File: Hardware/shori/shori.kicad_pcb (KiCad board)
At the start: 4 copper layers, 13 x 1.4 mm, 50 parts, among them J1 Conn_02x03_Top_Bottom, J2 SWD_Header, J3 UART_Header, J5 AudioJack3, U1 STM32F405RGT6, U2 AP2112K-3.3, U3 PCM3060PWR, U4 NE5532, Y1 16MHz

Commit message: Started General Component Layout
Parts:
- moved R2 118.0 mm to (167.8, 125.3), turned to -90 degrees
- moved R3 117.8 mm to (170.2, 125.3), turned to 90 degrees
- moved R1 103.9 mm to (163.8, 105.5), turned to 180 degrees
- moved J2 93.6 mm to (172.8, 100.1), turned to -90 degrees
- moved J3 91.3 mm to (135.0, 111.8), turned to -90 degrees
- moved C12 80.2 mm to (117.7, 98.7)
- moved C18 43.9 mm to (202.8, 116.2), turned to -90 degrees
- moved C15 41.7 mm to (220.5, 115.3), turned to -90 degrees
- moved U3 41.7 mm to (209.6, 116.0)
- moved C17 40.5 mm to (200.0, 116.3), turned to -90 degrees
- moved U1 38.8 mm to (166.5, 115.3)
- moved C16 38.2 mm to (215.8, 114.8), turned to -90 degrees

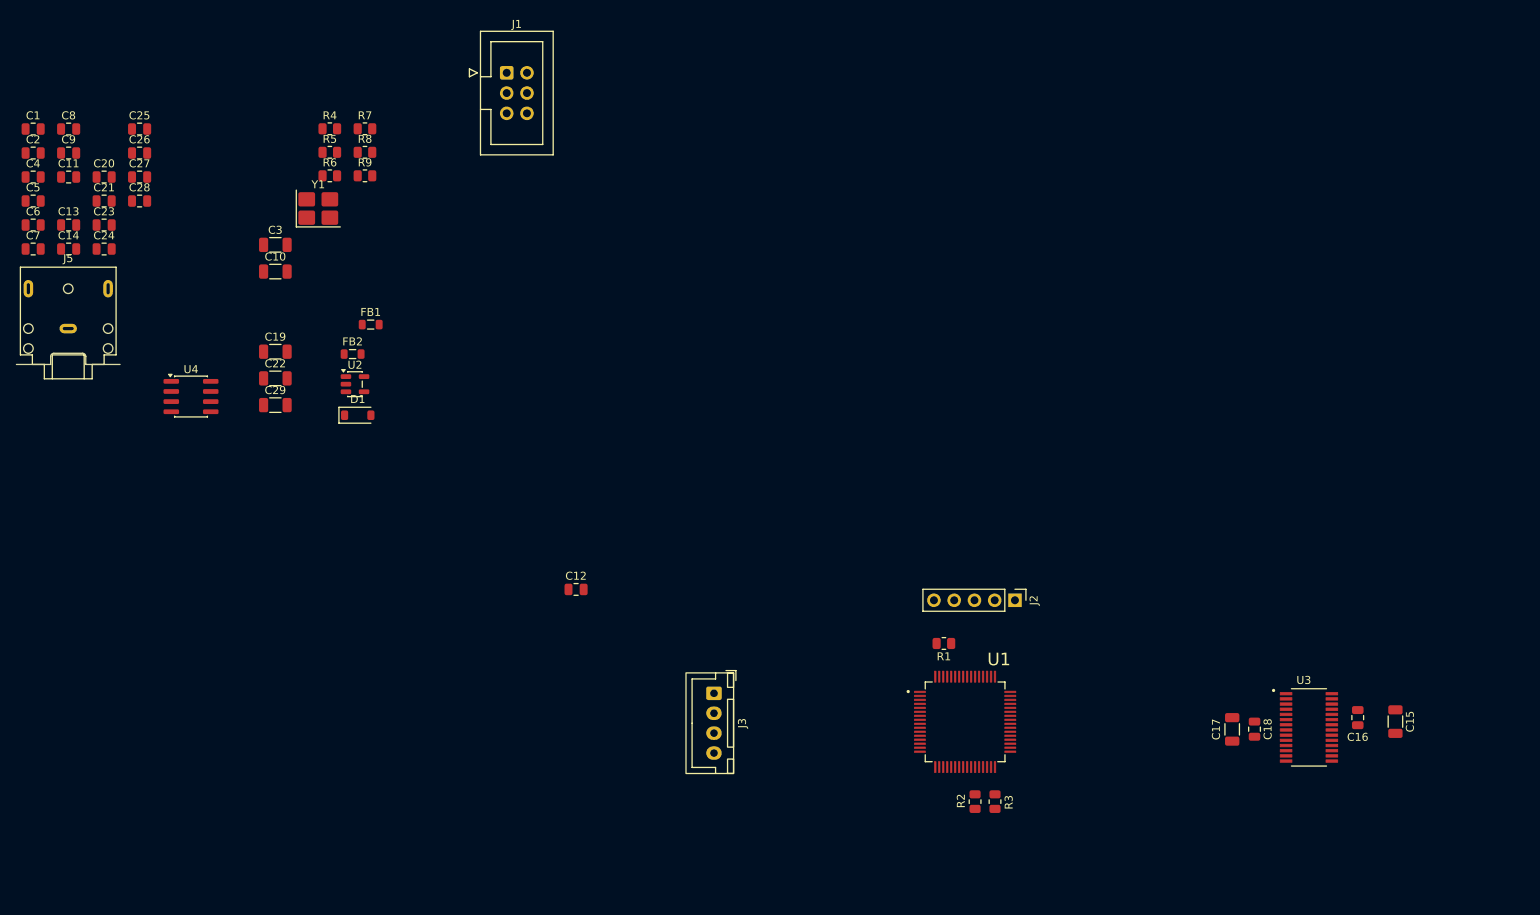
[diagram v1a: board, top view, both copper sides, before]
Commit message: Finished Layout on shori of digital components
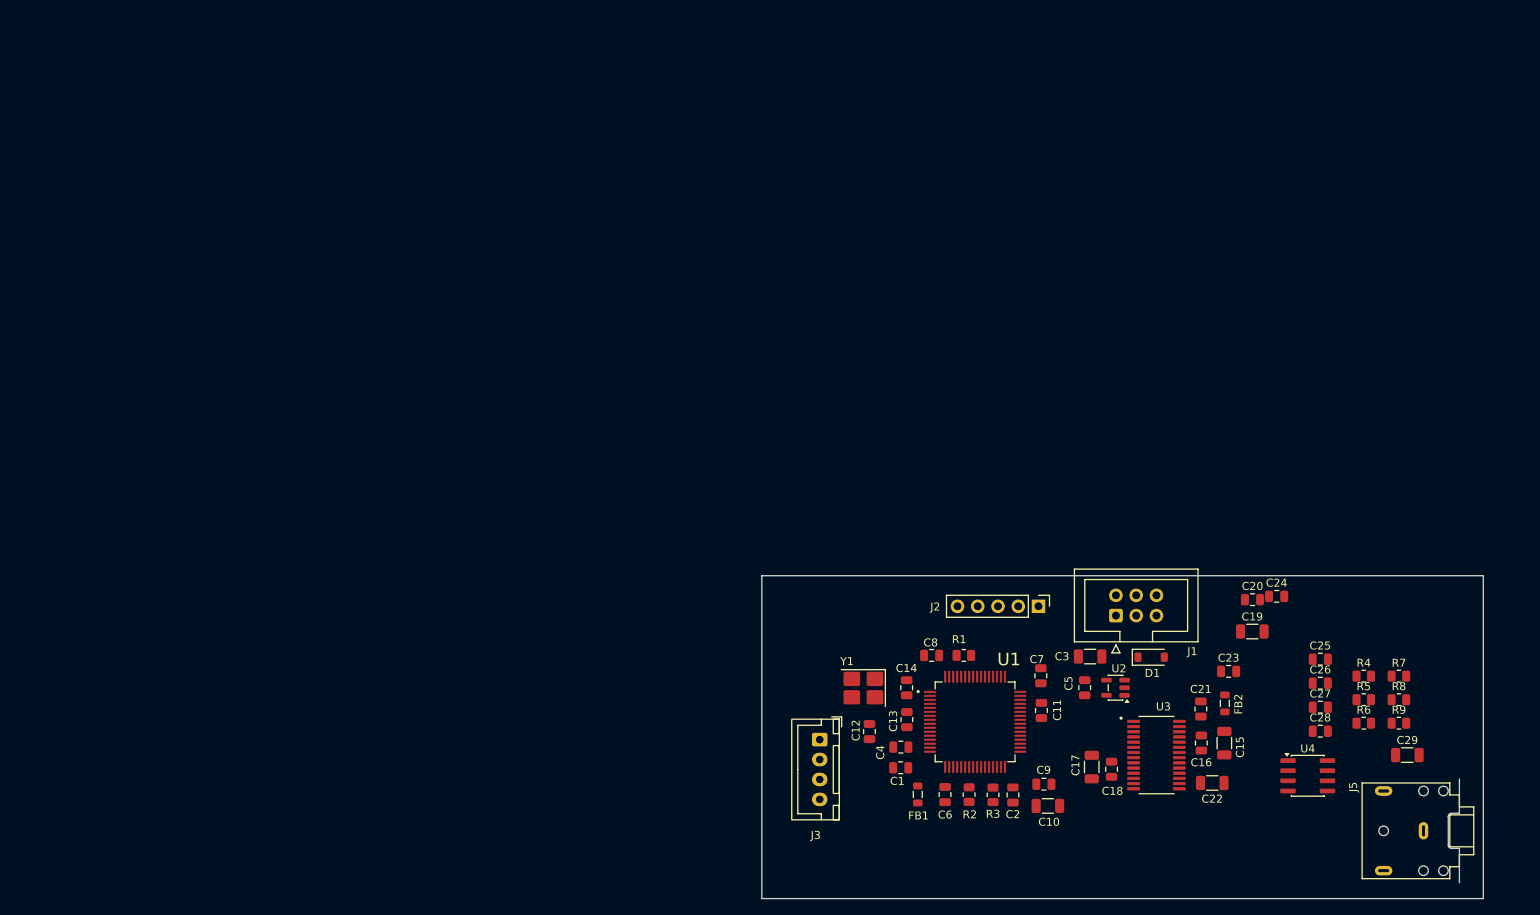
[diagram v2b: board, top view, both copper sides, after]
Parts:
- moved J5 181.3 mm to (224.0, 129.0), turned to 90 degrees
- moved C25 162.3 mm to (211.1, 107.5)
- moved C26 162.3 mm to (211.1, 110.5)
- moved C27 162.3 mm to (211.1, 113.5)
- moved C28 162.3 mm to (211.1, 116.5)
- moved C20 153.5 mm to (202.6, 100.0)
- moved C24 153.4 mm to (205.6, 99.6)
- moved C23 151.8 mm to (199.6, 109.0)
- moved C21 151.6 mm to (196.1, 113.7), turned to 90 degrees
- moved C29 148.6 mm to (222.0, 119.5)
- moved U4 147.9 mm to (209.5, 122.1)
- moved C2 146.9 mm to (172.5, 124.5), turned to 90 degrees
- moved R4 146.7 mm to (216.5, 109.6)
- moved R5 146.7 mm to (216.5, 112.5)
- moved R6 146.7 mm to (216.5, 115.5)
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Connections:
- net Net-(D1-K) renamed /INPUT_CAP_LDO
- J1 pad 1: +5V -> /AUDIO_IN
- J1 pad 3: /AUDIO_IN -> /AUDIO_OUT
- J1 pad 5: /AUDIO_OUT -> +5V
- J3 pad 1: +3.3V -> GND
- J3 pad 4: GND -> +3.3V
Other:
- board size 13 x 1.4 mm -> 90.5 x 40.5 mm

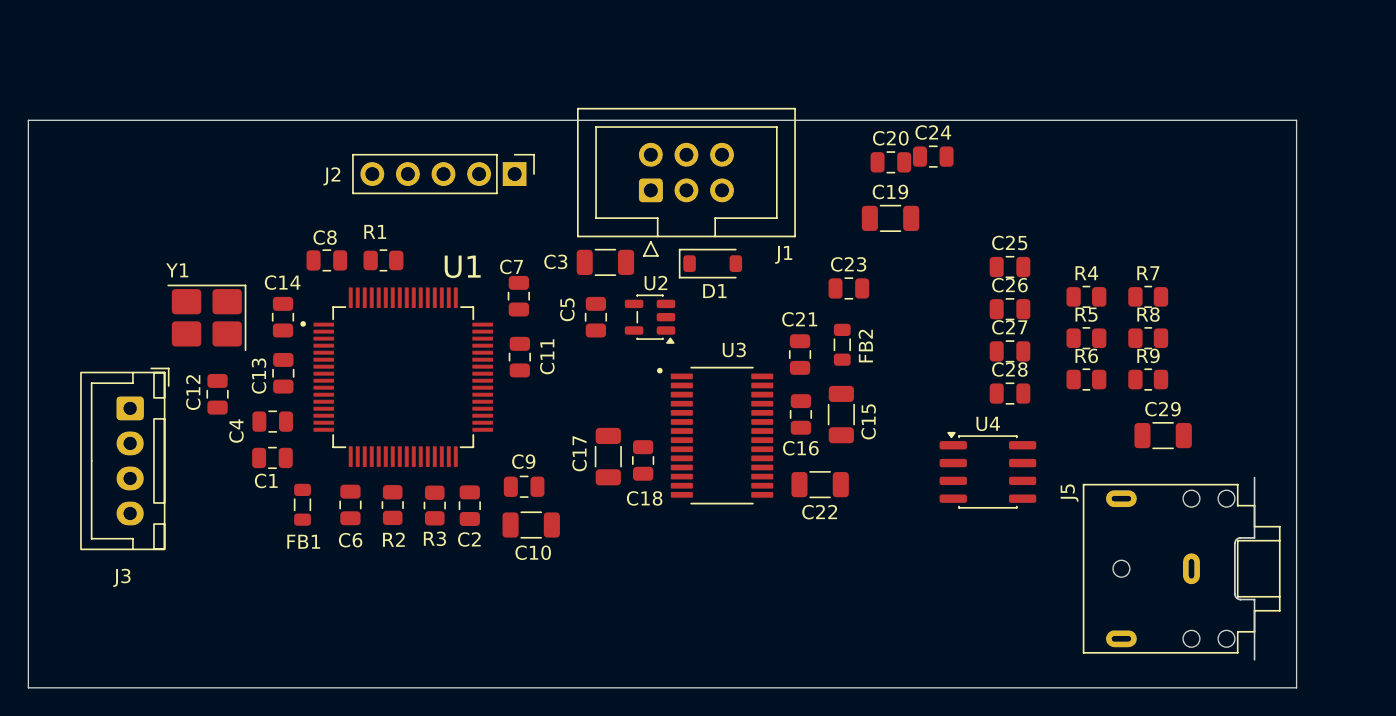
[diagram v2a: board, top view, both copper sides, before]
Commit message: Analog side layout complete on shori
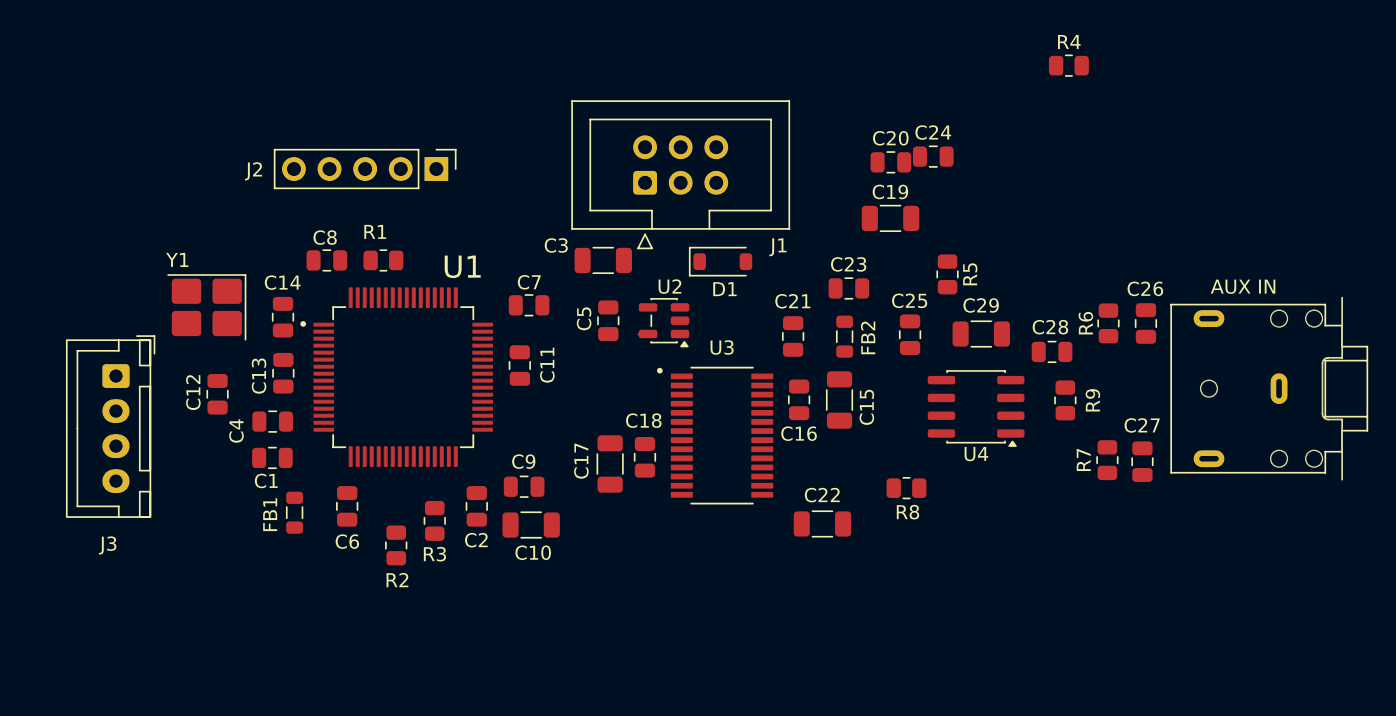
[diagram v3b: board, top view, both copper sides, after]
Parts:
- AUX IN: renamed from J5
- moved R8 20.3 mm to (203.7, 123.2)
- moved R4 16.5 mm to (215.3, 93.1)
- moved C29 14.9 mm to (209.0, 112.2), turned to 180 degrees
- moved AUX IN 14.3 mm to (230.2, 116.2)
- moved C27 12.3 mm to (220.5, 121.4), turned to 90 degrees
- moved R7 12.0 mm to (218.0, 121.2), turned to 90 degrees
- moved R5 10.9 mm to (206.6, 108.0), turned to -90 degrees
- moved C26 9.75 mm to (220.8, 111.5), turned to -90 degrees
- moved C25 8.61 mm to (203.9, 112.3), turned to 90 degrees
- moved R9 6.10 mm to (215.0, 117.0), turned to 90 degrees
- moved J2 5.60 mm to (170.1, 100.5)
- moved U4 4.73 mm to (208.6, 117.4), turned to 180 degrees
- moved R6 4.30 mm to (218.1, 111.5), turned to -90 degrees
- moved C28 4.22 mm to (214.1, 113.5), turned to 180 degrees
- moved R2 2.89 mm to (167.2, 127.3)
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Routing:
- net +3.3V: track 0.00 -> 0.71 mm
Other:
- board size 90.5 x 40.5 mm -> 1.4 x 13 mm

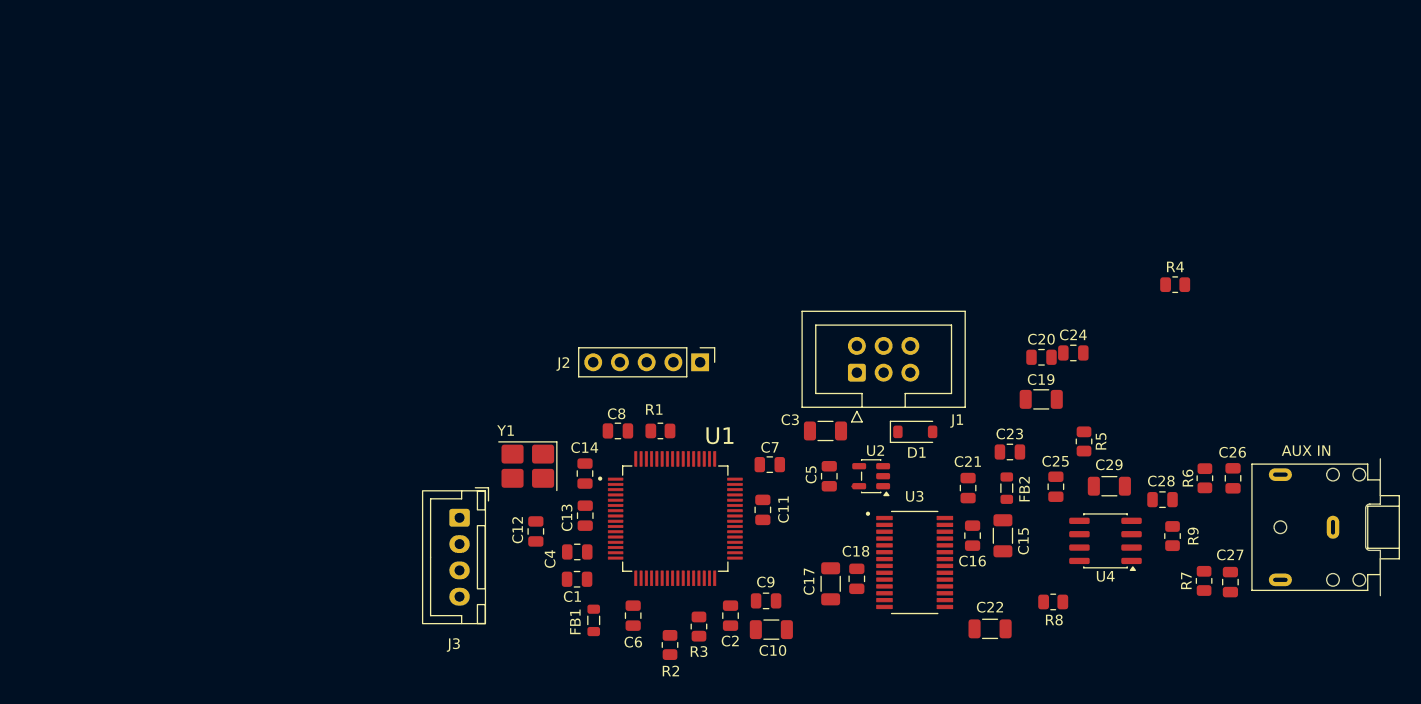
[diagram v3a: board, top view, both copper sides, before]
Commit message: Added Mounting holes and fixed Board outline issue
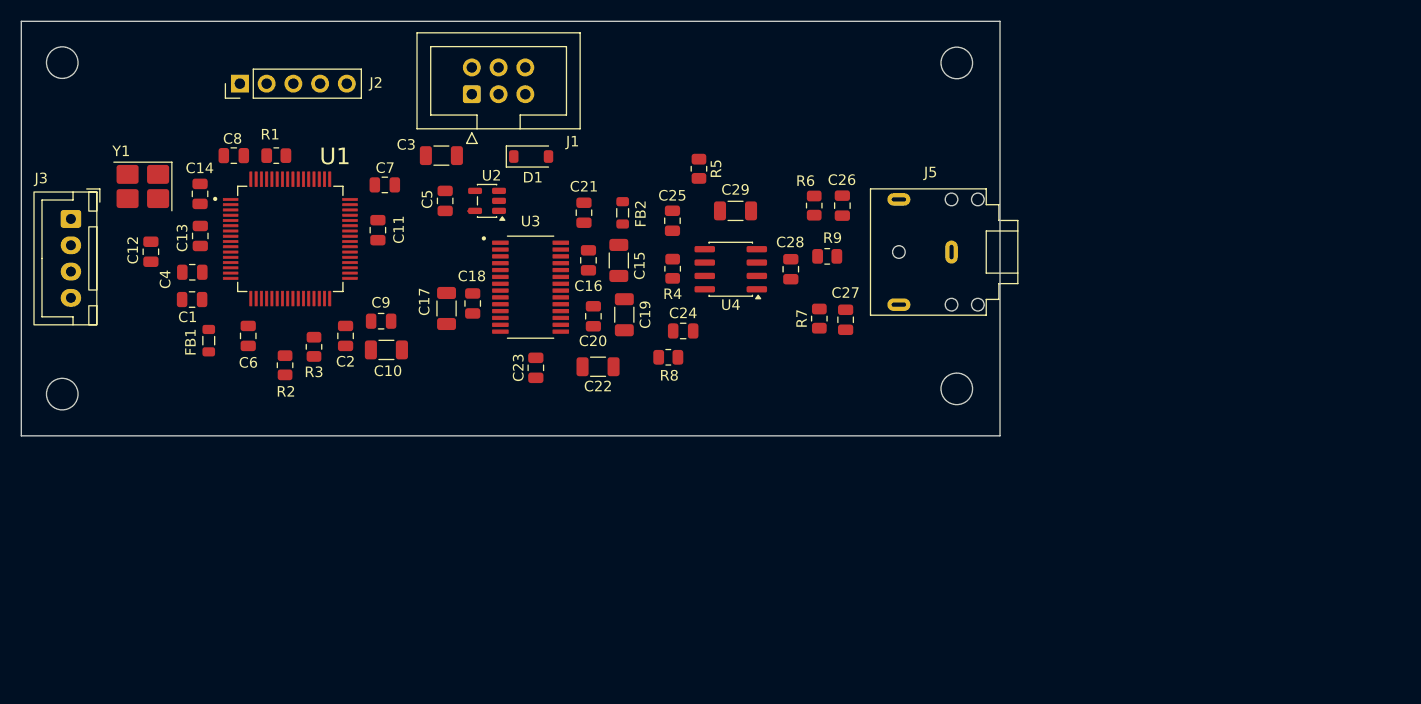
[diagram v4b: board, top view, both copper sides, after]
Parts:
- removed AUX IN: AudioJack3, Connector_Audio:Jack_3.5mm_CUI_SJ1-3523N_Horizontal
- added H1: MountingHole, MountingHole:MountingHole_3mm, F.Cu at (194.5, 72.0)
- added H2: MountingHole, MountingHole:MountingHole_3mm, F.Cu at (194.5, 103.0)
- added H3: MountingHole, MountingHole:MountingHole_3mm, F.Cu at (109.5, 72.0)
- added H4: MountingHole, MountingHole:MountingHole_3mm, F.Cu at (109.5, 103.5)
- added J5: AudioJack3, Connector_Audio:Jack_3.5mm_CUI_SJ1-3523N_Horizontal, F.Cu at (194.0, 90.0)
- moved J2 51.1 mm to (126.4, 74.0), turned to 90 degrees
- moved R4 47.8 mm to (167.5, 91.6), turned to 90 degrees
- moved J3 46.6 mm to (110.3, 86.9)
- moved C23 45.8 mm to (154.5, 101.0), turned to -90 degrees
- moved R6 45.3 mm to (181.0, 85.6)
- moved C26 45.3 mm to (183.6, 85.6)
- moved R2 45.2 mm to (130.7, 100.8)
- moved R3 45.2 mm to (133.4, 99.0)
- moved C10 45.2 mm to (140.3, 99.3)
- moved C2 45.2 mm to (136.4, 98.0)
- moved C7 45.2 mm to (140.2, 83.6)
- moved C9 45.2 mm to (139.8, 96.6)
- moved U1 45.2 mm to (131.2, 88.8)
- moved C1 45.2 mm to (121.8, 94.5)
- moved C12 45.2 mm to (117.9, 90.0)
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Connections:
- net /INPUT_CAP_LDO renamed Net-(D1-K)
- J1 pad 1: /AUDIO_IN -> +5V
- J1 pad 3: /AUDIO_OUT -> /AUDIO_IN
- J1 pad 5: +5V -> /AUDIO_OUT
- J3 pad 1: GND -> +3.3V
- J3 pad 4: +3.3V -> GND
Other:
- board size 1.4 x 13 mm -> 93 x 39.4 mm
